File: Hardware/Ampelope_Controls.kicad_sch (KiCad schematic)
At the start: 34 parts, among them J10 Audio1_Out, J11 Audio2_Out, J12 Audio3_Out, J13 Audio4_Out, J14 Env1_Out, J15 Env2_Out, J16 Env3_Out, J17 Env4_Out, J2 Gate1_In, J3 Gate2_In, J4 Gate3_In, J5 Gate4_In, J6 Audio1_In, J7 Audio2_In, J8 Audio3_In, J9 Audio4_In

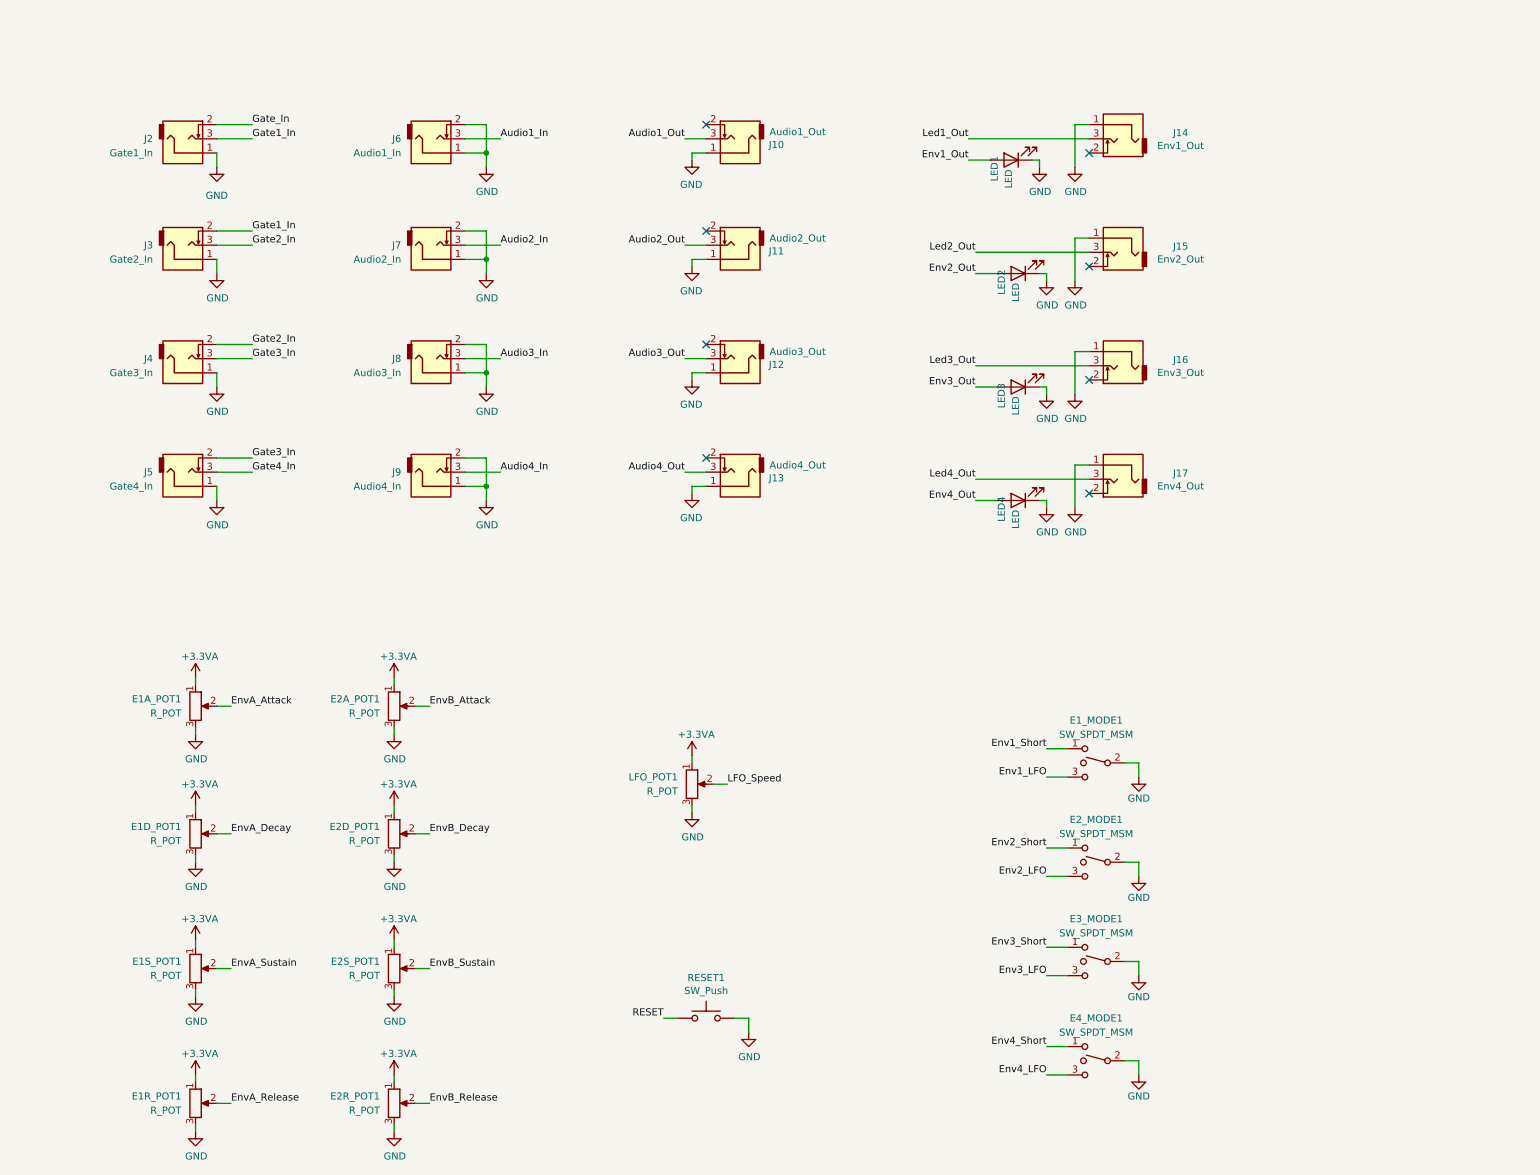
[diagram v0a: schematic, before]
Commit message: First Draft Layout of controls PCB
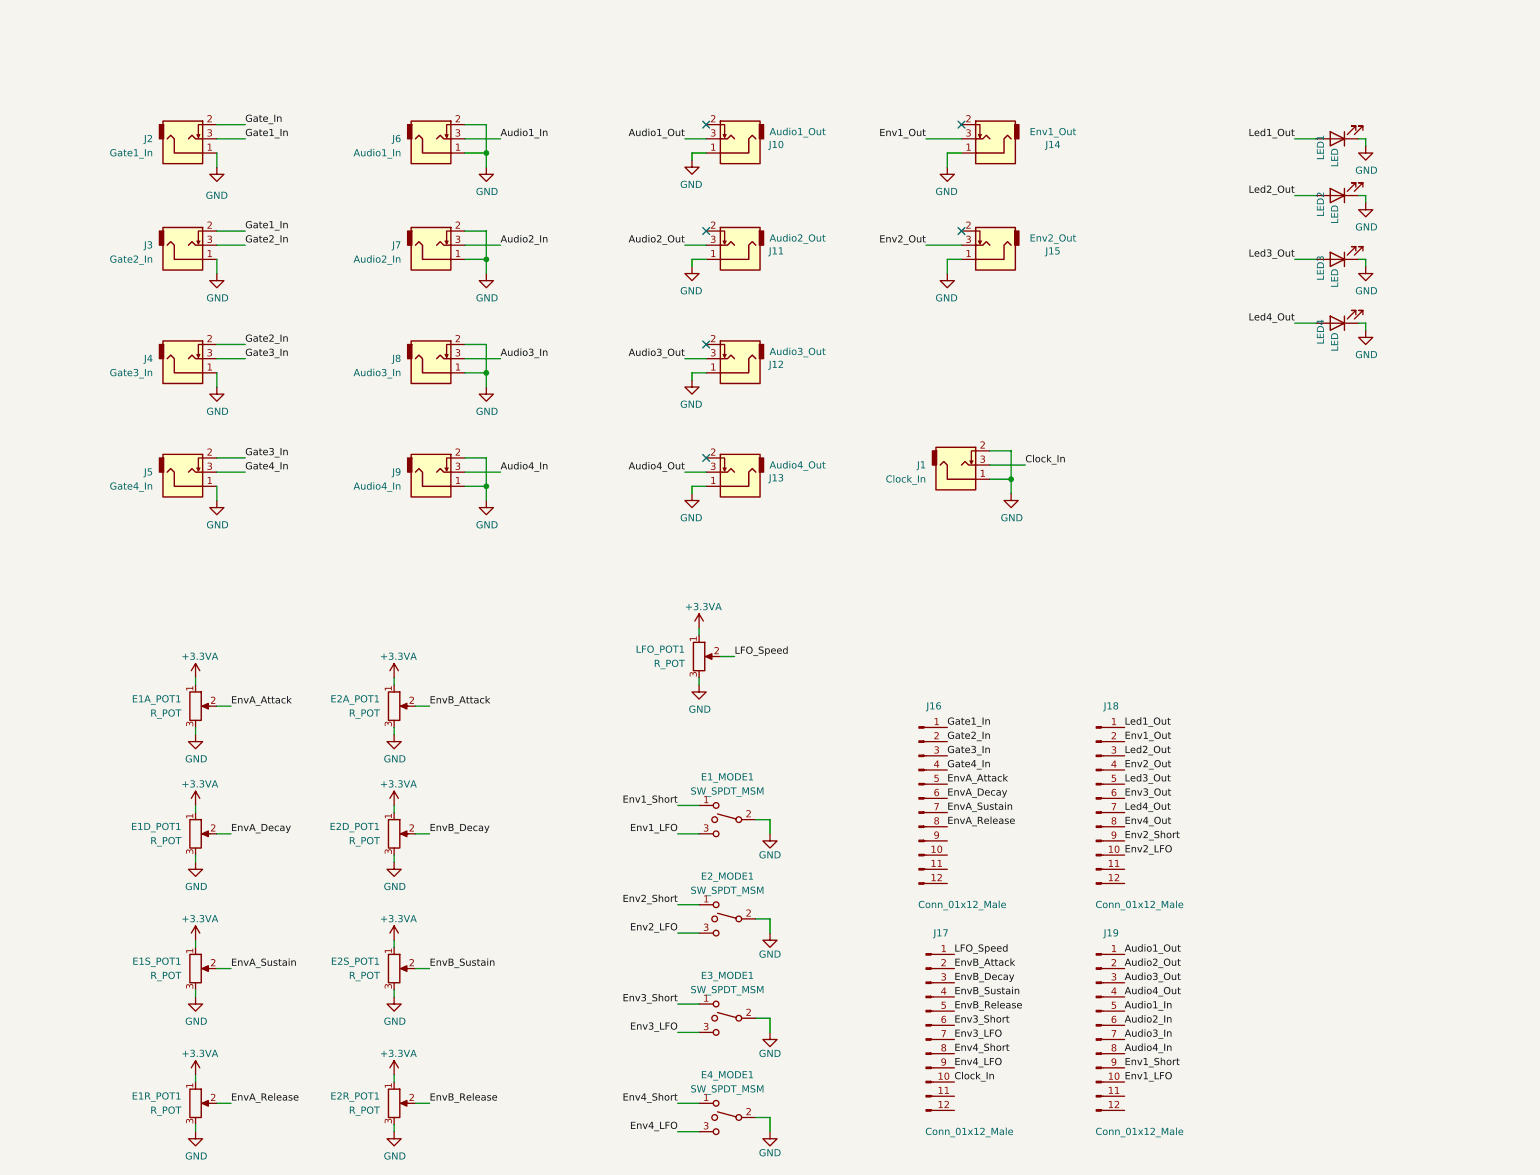
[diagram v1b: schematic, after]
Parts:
- removed J16: Env3_Out, Custom_Footprints:THONKICONN_hole, symbol thonkiconn:AudioJack2_Ground_Switch
- removed J17: Env4_Out, Custom_Footprints:THONKICONN_hole, symbol thonkiconn:AudioJack2_Ground_Switch
- removed RESET1: SW_Push, Custom_Footprints:SW_PUSH_6mm_aligned, symbol Switch:SW_Push
- added J1: Clock_In, Custom_Footprints:THONKICONN_hole, symbol thonkiconn:AudioJack2_Ground_Switch
- added J16, J17, J18, J19: Conn_01x12_Male, Connector_PinHeader_2.54mm:PinHeader_1x12_P2.54mm_Vertical, symbol Connector:Conn_01x12_Male
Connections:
- net Audio1_In: now also J19.5 (Pin_5)
- net Audio1_Out: now also J19.1 (Pin_1)
- net Audio2_In: now also J19.6 (Pin_6)
- net Audio2_Out: now also J19.2 (Pin_2)
- net Audio3_In: now also J19.7 (Pin_7)
- net Audio3_Out: now also J19.3 (Pin_3)
- net Audio4_In: now also J19.8 (Pin_8)
- net Audio4_Out: now also J19.4 (Pin_4)
- net Env1_LFO: now also J19.10 (Pin_10)
- net Env1_Out: now also J14.3, J18.2 (Pin_2); no longer LED1.2 (A)
- net Env1_Short: now also J19.9 (Pin_9)
- net Env2_LFO: now also J18.10 (Pin_10)
- net Env2_Out: now also J15.3, J18.4 (Pin_4); no longer LED2.2 (A)
- net Env2_Short: now also J18.9 (Pin_9)
- net Env3_LFO: now also J17.7 (Pin_7)
- net Env3_Out: now also J18.6 (Pin_6); no longer LED3.2 (A)
- net Env3_Short: now also J17.6 (Pin_6)
- net Env4_LFO: now also J17.9 (Pin_9)
- net Env4_Out: now also J18.8 (Pin_8); no longer LED4.2 (A)
- net Env4_Short: now also J17.8 (Pin_8)
- net EnvA_Attack: now also J16.5 (Pin_5)
- net EnvA_Decay: now also J16.6 (Pin_6)
- net EnvA_Release: now also J16.8 (Pin_8)
- net EnvA_Sustain: now also J16.7 (Pin_7)
- net EnvB_Attack: now also J17.2 (Pin_2)
- net EnvB_Decay: now also J17.3 (Pin_3)
- net EnvB_Release: now also J17.5 (Pin_5)
- net EnvB_Sustain: now also J17.4 (Pin_4)
- net GND: now also J1.1, J1.2
- net Gate1_In: now also J16.1 (Pin_1)
- net Gate2_In: now also J16.2 (Pin_2)
- net Gate3_In: now also J16.3 (Pin_3)
- net Gate4_In: now also J16.4 (Pin_4)
- net LFO_Speed: now also J17.1 (Pin_1)
- net Led1_Out: now also LED1.2 (A), J18.1 (Pin_1); no longer J14.3
- net Led2_Out: now also LED2.2 (A), J18.3 (Pin_3); no longer J15.3
- net Led3_Out: now also LED3.2 (A), J18.5 (Pin_5)
- net Led4_Out: now also LED4.2 (A), J18.7 (Pin_7)
- new net Clock_In: J1.3, J17.10 (Pin_10)
- no-connect marks 8 -> 6
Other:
- moved on the sheet: E1_MODE1, E2_MODE1, E3_MODE1, E4_MODE1, J14, J15, LED1, LED2, LED3, LED4, LFO_POT1

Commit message: Started rough placement of component board
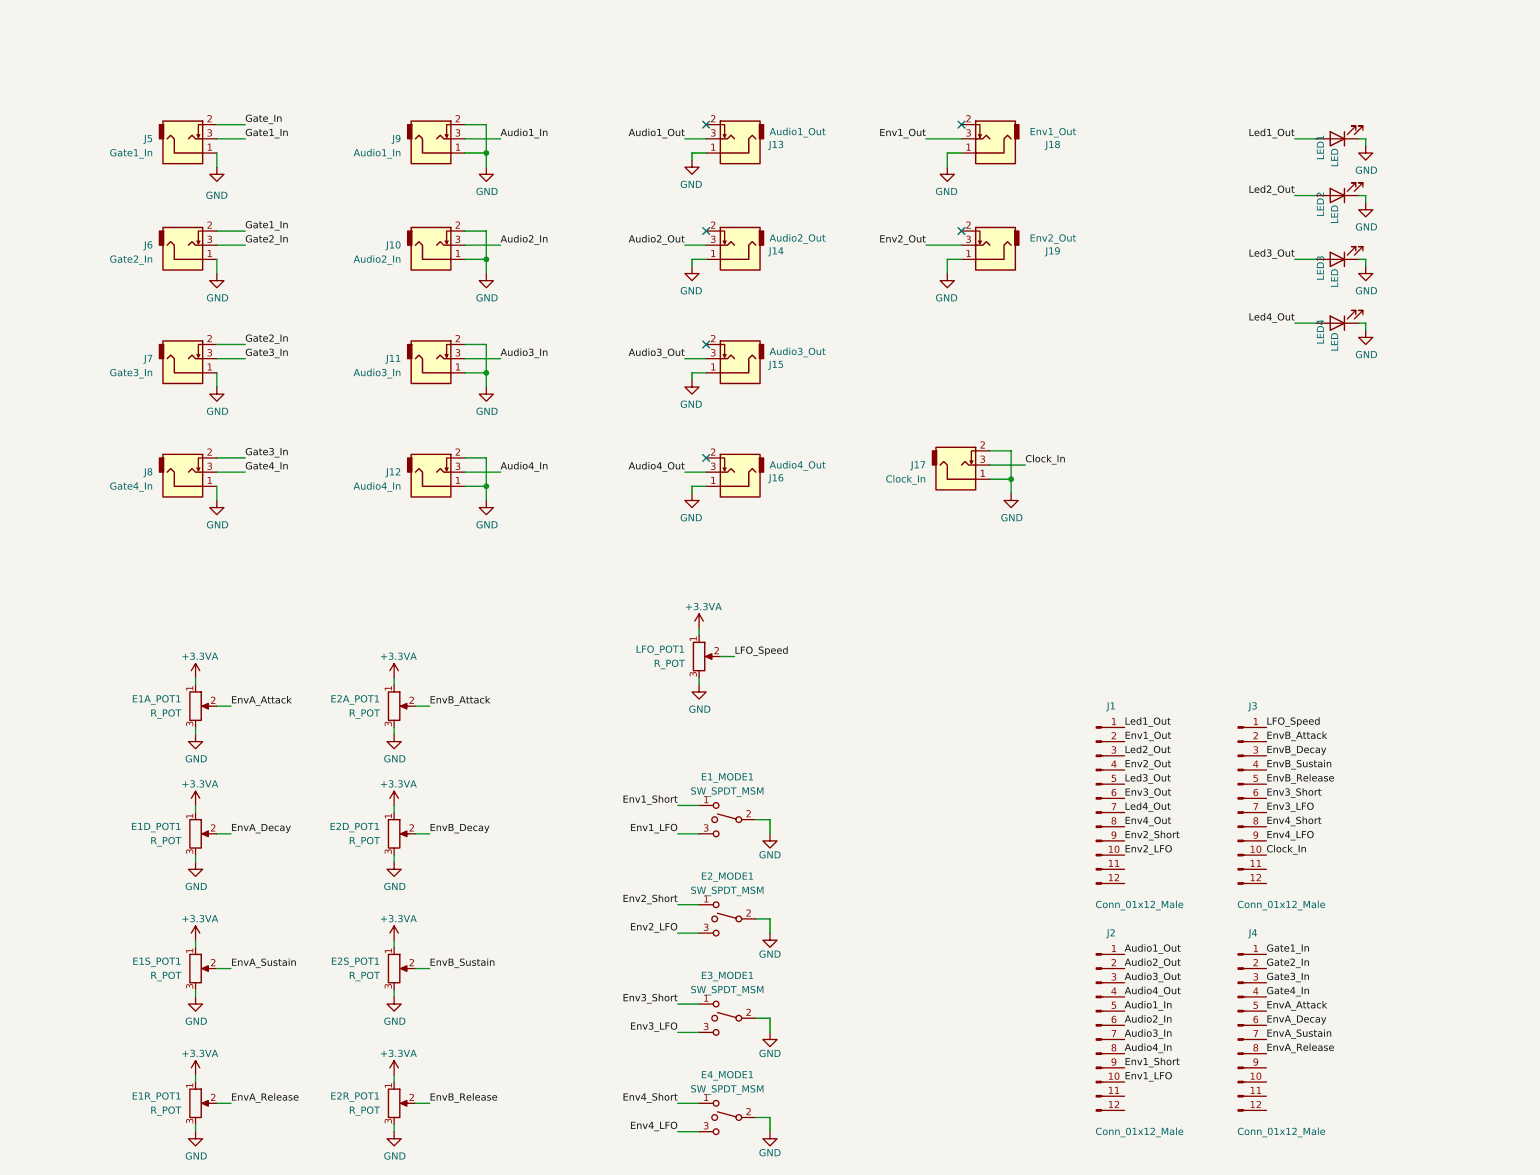
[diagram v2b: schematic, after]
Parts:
- renumbered J18 to J1, J7 to J10, J8 to J11, J9 to J12, J10 to J13, J11 to J14, J12 to J15, J13 to J16, J1 to J17, J14 to J18, J15 to J19, J19 to J2, J17 to J3, J16 to J4, J2 to J5, J3 to J6, J4 to J7, J5 to J8, J6 to J9
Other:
- moved on the sheet: J3, J4

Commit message: Layout on component board
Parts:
- J19: value Env2_Out -> Env3_Out
- LED1, LED2, LED3, LED4: footprint LED_THT:LED_D3.0mm -> Custom_Footprints:LED_D3.0mm
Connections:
- net Env2_Out: no longer J19.3
- net Env3_Out: now also J19.3
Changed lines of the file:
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@@
-(kicad_sch (version 20210621) (generator eeschema)
+(kicad_sch (version 20210615) (generator eeschema)
   (paper "A3")
   (junction (at 97.79 38.1) (diameter 1.016) (color 0 0 0 0))
@@
     (effects (font (size 1.27 1.27)) (justify right bottom))
   )
-  (label "Env2_Out" (at 176.53 54.61 180)
+  (label "Env3_Out" (at 176.53 54.61 180)
     (effects (font (size 1.27 1.27)) (justify right bottom))
   )
@@
       (effects (font (size 1.27 1.27)) (justify right))
     )
-    (property "Footprint" "LED_THT:LED_D3.0mm" (id 2) (at 250.19 35.56 0)
+    (property "Footprint" "Custom_Footprints:LED_D3.0mm" (id 2) (at 250.19 35.56 0)
       (effects (font (size 1.27 1.27)) hide)
     )
@@
       (effects (font (size 1.27 1.27)) (justify right))
     )
-    (property "Footprint" "LED_THT:LED_D3.0mm" (id 2) (at 250.19 45.72 0)
+    (property "Footprint" "Custom_Footprints:LED_D3.0mm" (id 2) (at 250.19 45.72 0)
       (effects (font (size 1.27 1.27)) hide)
     )
@@
       (effects (font (size 1.27 1.27)) (justify right))
     )
-    (property "Footprint" "LED_THT:LED_D3.0mm" (id 2) (at 250.19 57.15 0)
+    (property "Footprint" "Custom_Footprints:LED_D3.0mm" (id 2) (at 250.19 57.15 0)
       (effects (font (size 1.27 1.27)) hide)
     )
@@
       (effects (font (size 1.27 1.27)) (justify right))
     )
-    (property "Footprint" "LED_THT:LED_D3.0mm" (id 2) (at 250.19 68.58 0)
+    (property "Footprint" "Custom_Footprints:LED_D3.0mm" (id 2) (at 250.19 68.58 0)
       (effects (font (size 1.27 1.27)) hide)
     )
@@
     (in_bom yes) (on_board yes)
     (property "Reference" "J19" (id 0) (at 199.263 55.6768 0))
-    (property "Value" "Env2_Out" (id 1) (at 199.263 53.3654 0))
+    (property "Value" "Env3_Out" (id 1) (at 199.263 53.3654 0))
     (property "Footprint" "Custom_Footprints:THONKICONN_hole" (id 2) (at 187.96 54.61 0)
       (effects (font (size 1.27 1.27)) hide)
@@
     )
     (path "/cd966f67-1087-4aae-9be2-e22350ebac12"
-      (reference "J19") (unit 1) (value "Env2_Out") (footprint "Custom_Footprints:THONKICONN_hole")
+      (reference "J19") (unit 1) (value "Env3_Out") (footprint "Custom_Footprints:THONKICONN_hole")
     )
     (path "/e154c67c-bda2-4c7e-8d61-83db522f7a70"
-      (reference "LED1") (unit 1) (value "LED") (footprint "LED_THT:LED_D3.0mm")
+      (reference "LED1") (unit 1) (value "LED") (footprint "Custom_Footprints:LED_D3.0mm")
     )
     (path "/61ab5e10-f3bf-4b41-8224-59d53eb3c38b"
-      (reference "LED2") (unit 1) (value "LED") (footprint "LED_THT:LED_D3.0mm")
+      (reference "LED2") (unit 1) (value "LED") (footprint "Custom_Footprints:LED_D3.0mm")
     )
     (path "/5b95e2ef-93bb-44ec-842f-d7d3c34ee7e9"
-      (reference "LED3") (unit 1) (value "LED") (footprint "LED_THT:LED_D3.0mm")
+      (reference "LED3") (unit 1) (value "LED") (footprint "Custom_Footprints:LED_D3.0mm")
     )
     (path "/5d6e0c08-b975-49db-a052-9fc57cb5f17d"
-      (reference "LED4") (unit 1) (value "LED") (footprint "LED_THT:LED_D3.0mm")
+      (reference "LED4") (unit 1) (value "LED") (footprint "Custom_Footprints:LED_D3.0mm")
     )
     (path "/f31012a2-8253-4432-bcb4-c3546767352f"
